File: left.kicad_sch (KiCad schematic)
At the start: 65 parts, among them J3 LEFT, Q1 IRF540N, Q2 IRF540N, Q3 IRF540N, Q4 IRF540N, U1 TL072, U2 TL072, U4 LT1016, U5 IR2184, U6 IR2184

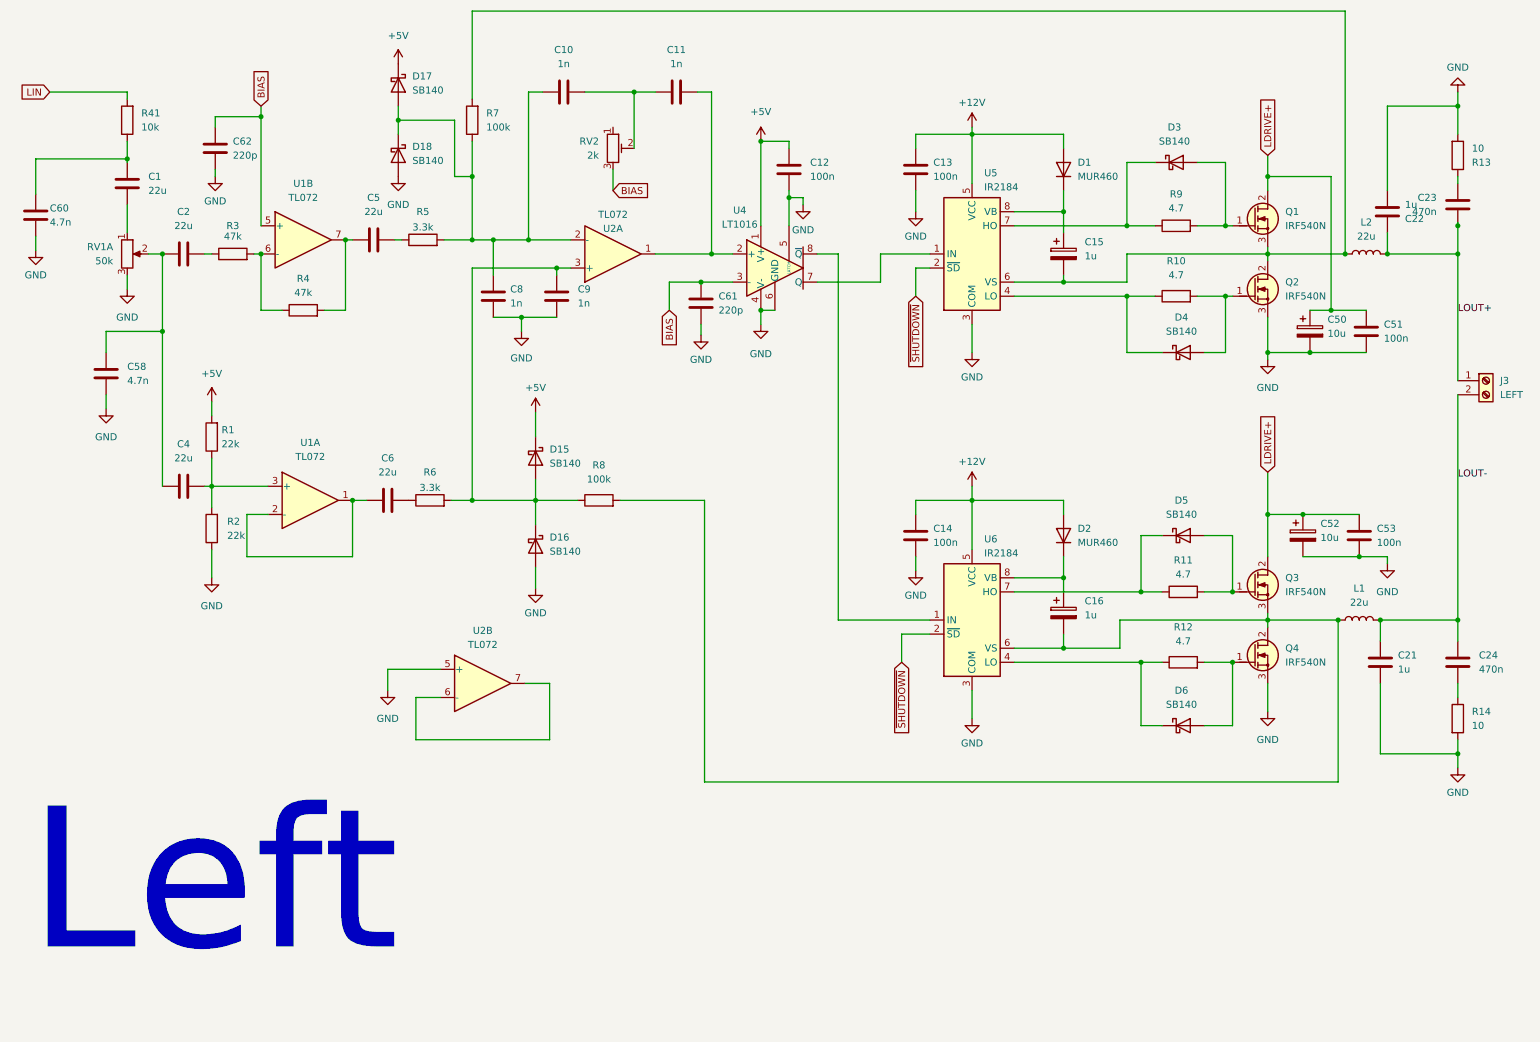
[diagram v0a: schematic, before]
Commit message: Recovered PCB
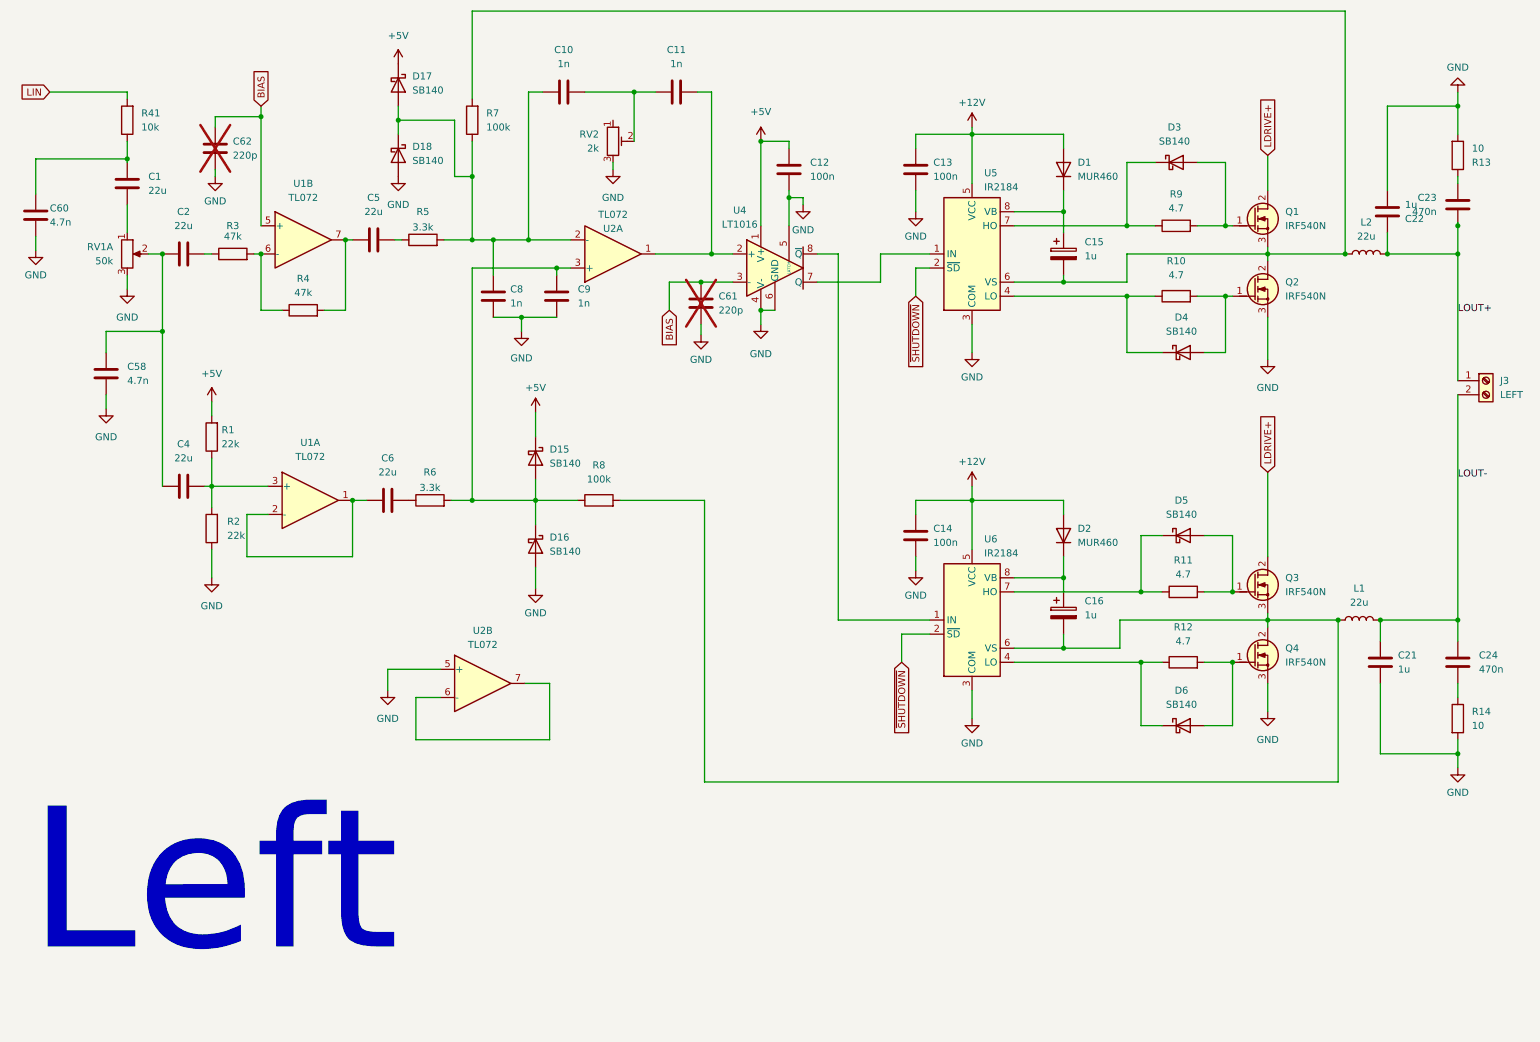
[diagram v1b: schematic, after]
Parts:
- removed C50, C52: 10u, Capacitor_THT:CP_Radial_D5.0mm_P2.50mm, symbol Device:C_Polarized
- removed C51, C53: 100n, Capacitor_THT:C_Disc_D3.4mm_W2.1mm_P2.50mm, symbol Device:C
- C61, C62: now not fitted
- RV2: footprint Potentiometer_THT:TRIM_3362P-1-253LF -> Potentiometer_THT:Potentiometer_Runtron_RM-065_Vertical
- U1, U2, U4, U5, U6: footprint PCM_Package_DIP_AKL:DIP-8_W7.62mm -> Package_DIP:DIP-8_W7.62mm_LongPads
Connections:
- net BIAS: no longer RV2.3
- net GND: now also RV2.3
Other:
- moved on the sheet: RV2
